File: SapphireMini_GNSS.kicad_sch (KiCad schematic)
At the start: 20 parts, among them J401 Conn_01x01_Male, U401 TPS22860DBVR, U402 SAM-M8Q-0-10

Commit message: Corrected to get clean review on schematic
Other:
- title: Sapphire Mini -> Sapphire Mini M2
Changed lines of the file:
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@@
   (paper "USLetter")
   (title_block
-    (title "Sapphire Mini")
+    (title "Sapphire Mini M2")
+    (date "2022-09-26")
+    (rev "1")
     (company "Southern Methodist Univ")
+    (comment 1 "Chris Hayward")
   )
   (junction (at 118.11 46.99) (diameter 0) (color 0 0 0 0)

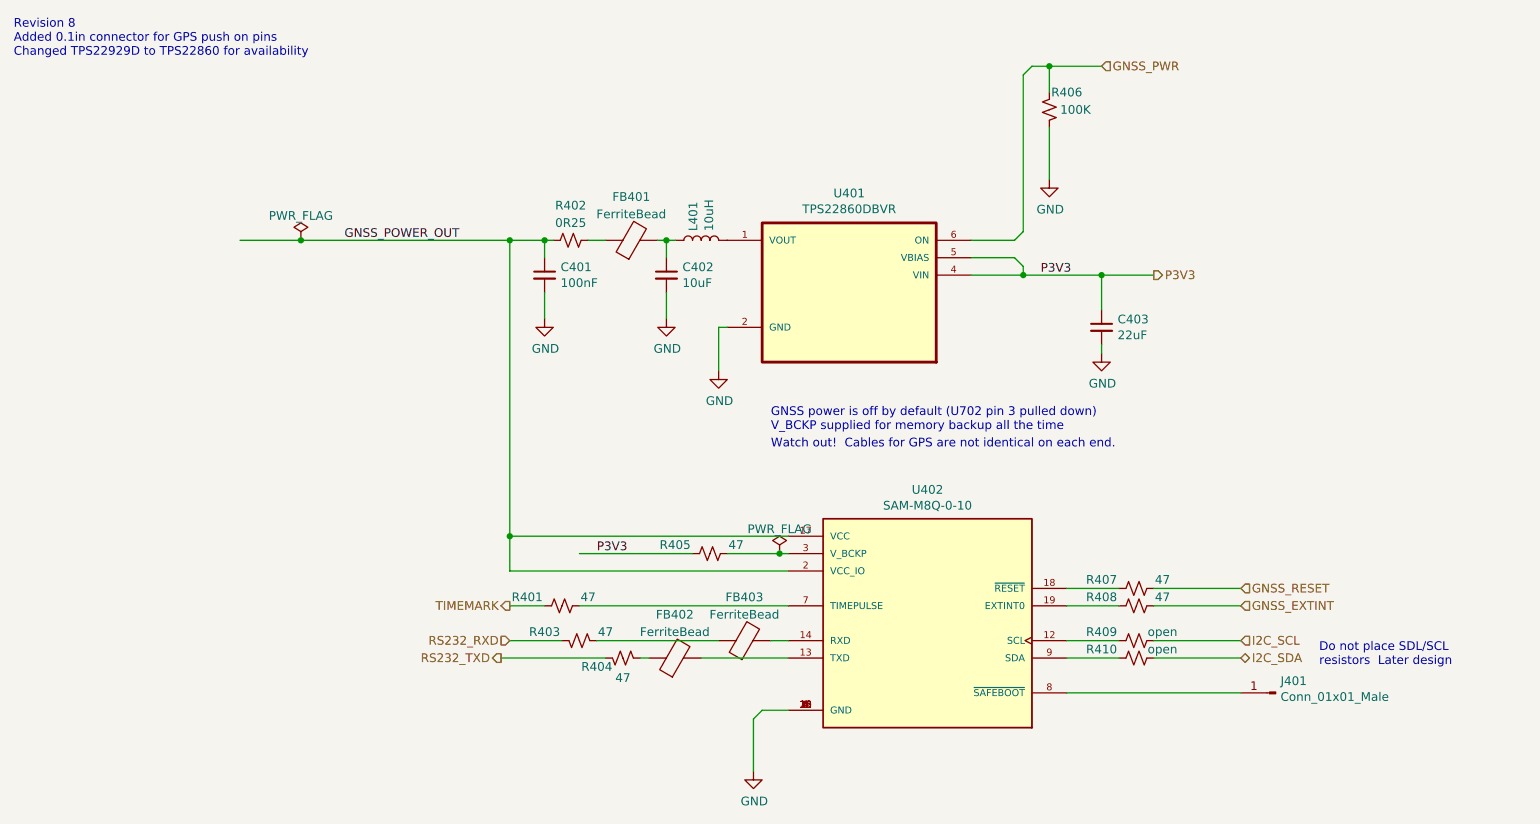
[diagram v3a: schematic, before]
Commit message: Footprints complete. Starting layout
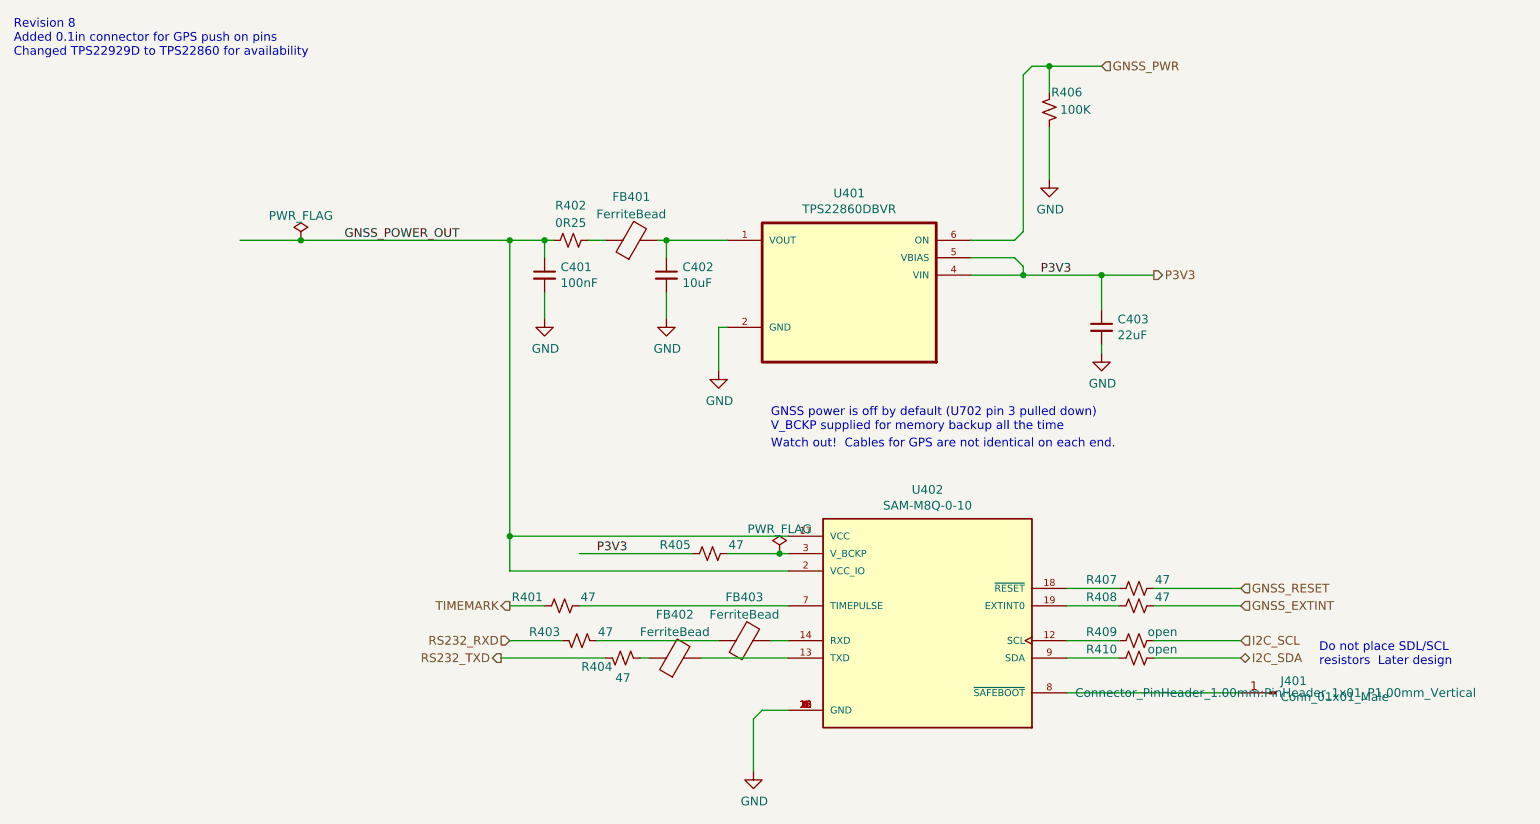
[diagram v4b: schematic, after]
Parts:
- removed L401: 10uH, symbol Device:L
- C401: MPN CL10B104KA8NNNC -> CL05A104KA5NNNC
- C402: MPN CL21B105KOFNNNG -> CL21A106KAYNNNE
- C403: MPN CGA5L1X5R1C226M160AC -> CL21A226MAYNNNE; Manufacturer TDK -> Samsung
- FB401, FB402, FB403: footprint (none) -> Inductor_SMD:L_0201_0603Metric; MPN (none) -> BLM18AG221SN1D
- J401: footprint (none) -> Connector_PinHeader_1.00mm:PinHeader_1x01_P1.00mm_Vertical; MPN (none) -> DNP
- U402: MPN (none) -> SAM-M8Q-0-10; Manufacturer (none) -> u-blox
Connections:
- net at C402.1, FB401.2: now also U401.1 (VOUT)
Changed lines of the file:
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@@
     (stroke (width 0) (type default) (color 0 0 0 0))
   )
-  (wire (pts (xy 118.11 46.99) (xy 119.38 46.99))
+  (wire (pts (xy 118.11 46.99) (xy 127 46.99))
     (stroke (width 0) (type default) (color 0 0 0 0))
   )
@@
       (effects (font (size 1.27 1.27)) hide)
     )
-    (property "MPN" "CL10B104KA8NNNC" (id 5) (at 100.33 52.07 0)
+    (property "MPN" "CL05A104KA5NNNC" (id 5) (at 100.33 52.07 0)
       (effects (font (size 1.27 1.27)) hide)
     )
@@
       (effects (font (size 1.27 1.27)) hide)
     )
-    (property "Description" "0.1 µF ±10% 25V Ceramic Capacitor X7R 0603 (1608 Metric)" (id 15) (at 100.33 52.07 0)
+    (property "Description" "0.1 µF ±10% 25V Ceramic Capacitor X5R 0402 (1005 Metric)" (id 15) (at 100.33 52.07 0)
       (effects (font (size 1.27 1.27)) hide)
     )
@@
       (effects (font (size 1.27 1.27)) hide)
     )
-    (property "MPN" "CGA5L1X5R1C226M160AC" (id 5) (at 181.61 59.69 0)
-      (effects (font (size 1.27 1.27)) hide)
-    )
-    (property "Manufacturer" "TDK" (id 6) (at 181.61 59.69 0)
+    (property "MPN" "CL21A226MAYNNNE" (id 5) (at 181.61 59.69 0)
+      (effects (font (size 1.27 1.27)) hide)
+    )
+    (property "Manufacturer" "Samsung" (id 6) (at 181.61 59.69 0)
       (effects (font (size 1.27 1.27)) hide)
     )
@@
       (effects (font (size 1.27 1.27)) hide)
     )
-    (property "Description" "22 µF ±20% 16V Ceramic Capacitor X5R 1206" (id 15) (at 181.61 59.69 0)
+    (property "Description" "22 µF ±20% 25V Ceramic Capacitor X5R 0805 (2012 Metric)" (id 15) (at 181.61 59.69 0)
       (effects (font (size 1.27 1.27)) hide)
     )
@@
       (effects (font (size 1.27 1.27)) hide)
     )
-    (property "MPN" "CL21B105KOFNNNG" (id 5) (at 118.11 52.07 0)
+    (property "MPN" "CL21A106KAYNNNE" (id 5) (at 118.11 52.07 0)
       (effects (font (size 1.27 1.27)) hide)
     )
@@
       (effects (font (size 1.27 1.27)) hide)
     )
-    (property "Description" "1 µF ±10% 16V Ceramic Capacitor X7R 0805 " (id 15) (at 118.11 52.07 0)
+    (property "Description" "10 µF ±10% 25V Ceramic Capacitor X5R 0805 (2012 Metric)" (id 15) (at 118.11 52.07 0)
       (effects (font (size 1.27 1.27)) hide)
     )
@@
     (property "MAXIMUM_PACKAGE_HEIGHT" "6.80mm" (id 7) (at 156.21 102.87 0)
       (effects (font (size 1.27 1.27)) (justify left bottom) hide)
+    )
+    (property "Description" "RF RX GALILEO 1.575GHZ/1.602GHZ" (id 8) (at 156.21 102.87 0)
+      (effects (font (size 1.27 1.27)) hide)
+    )
+    (property "MPN" "SAM-M8Q-0-10" (id 9) (at 156.21 102.87 0)
+      (effects (font (size 1.27 1.27)) hide)
+    )
+    (property "Manufacturer" "u-blox" (id 10) (at 156.21 102.87 0)
+      (effects (font (size 1.27 1.27)) hide)
     )
     (pin "1")
@@
       (effects (font (size 1.27 1.27)) (justify right))
     )
-    (property "Footprint" "" (id 2) (at 207.01 113.03 0)
-      (effects (font (size 1.27 1.27)) hide)
-    )
+    (property "Footprint" "Connector_PinHeader_1.00mm:PinHeader_1x01_P1.00mm_Vertical" (id 2) (at 207.01 113.03 0))
     (property "Datasheet" "~" (id 3) (at 207.01 113.03 0)
       (effects (font (size 1.27 1.27)) hide)
     )
-    (pin "1")
-  )
-  (symbol (lib_id "Device:L") (at 123.19 46.99 90) (unit 1)
-    (in_bom yes) (on_board yes)
-    (property "Reference" "L401" (id 0) (at 122.0216 45.6438 0)
-      (effects (font (size 1.27 1.27)) (justify left))
-    )
-    (property "Value" "10uH" (id 1) (at 124.333 45.6438 0)
-      (effects (font (size 1.27 1.27)) (justify left))
-    )
-    (property "Footprint" "" (id 2) (at 123.19 46.99 0)
-      (effects (font (size 1.27 1.27)) hide)
-    )
-    (property "Datasheet" "~" (id 3) (at 123.19 46.99 0)
-      (effects (font (size 1.27 1.27)) hide)
-    )
-    (pin "1")
-    (pin "2")
+    (property "Description" "PPS connector" (id 4) (at 207.01 113.03 0)
+      (effects (font (size 1.27 1.27)) hide)
+    )
+    (property "MPN" "DNP" (id 5) (at 207.01 113.03 0)
+      (effects (font (size 1.27 1.27)) hide)
+    )
+    (pin "1")
   )
   (symbol (lib_id "Device:R_Small_US") (at 104.14 46.99 90) (unit 1)
@@
     )
     (pin "1")
+  )
+  (symbol (lib_id "Device:FerriteBead") (at 129.54 105.41 90) (unit 1)
+    (in_bom yes) (on_board yes) (fields_autoplaced)
+    (property "Reference" "FB403" (id 0) (at 129.4892 99.0686 90))
+    (property "Value" "FerriteBead" (id 1) (at 129.4892 101.6055 90))
+    (property "Footprint" "Inductor_SMD:L_0201_0603Metric" (id 2) (at 129.54 107.188 90)
+      (effects (font (size 1.27 1.27)) hide)
+    )
+    (property "Datasheet" "~" (id 3) (at 129.54 105.41 0)
+      (effects (font (size 1.27 1.27)) hide)
+    )
+    (property "Description" "220 Ohms @ 100 MHz 1 Ferrite Bead 0603 (1608 Metric) 500mA 250mOhm" (id 4) (at 129.54 105.41 0)
+      (effects (font (size 1.27 1.27)) hide)
+    )
+    (property "MPN" "BLM18AG221SN1D" (id 5) (at 129.54 105.41 0)
+      (effects (font (size 1.27 1.27)) hide)
+    )
+    (pin "1")
+    (pin "2")
   )
   (symbol (lib_id "Device:FerriteBead") (at 113.03 46.99 90) (unit 1)
@@
     (property "Reference" "FB401" (id 0) (at 112.9792 40.6486 90))
     (property "Value" "FerriteBead" (id 1) (at 112.9792 43.1855 90))
-    (property "Footprint" "" (id 2) (at 113.03 48.768 90)
+    (property "Footprint" "Inductor_SMD:L_0201_0603Metric" (id 2) (at 113.03 48.768 90)
       (effects (font (size 1.27 1.27)) hide)
     )
@@
       (effects (font (size 1.27 1.27)) hide)
     )
-    (pin "1")
-    (pin "2")
-  )
-  (symbol (lib_id "Device:FerriteBead") (at 129.54 105.41 90) (unit 1)
-    (in_bom yes) (on_board yes) (fields_autoplaced)
-    (property "Reference" "FB403" (id 0) (at 129.4892 99.0686 90))
-    (property "Value" "FerriteBead" (id 1) (at 129.4892 101.6055 90))
-    (property "Footprint" "" (id 2) (at 129.54 107.188 90)
-      (effects (font (size 1.27 1.27)) hide)
-    )
-    (property "Datasheet" "~" (id 3) (at 129.54 105.41 0)
+    (property "Description" "220 Ohms @ 100 MHz 1 Ferrite Bead 0603 (1608 Metric) 500mA 250mOhm" (id 4) (at 113.03 46.99 0)
+      (effects (font (size 1.27 1.27)) hide)
+    )
+    (property "MPN" "BLM18AG221SN1D" (id 5) (at 113.03 46.99 0)
       (effects (font (size 1.27 1.27)) hide)
     )
@@
     (property "Reference" "FB402" (id 0) (at 119.3292 101.6086 90))
     (property "Value" "FerriteBead" (id 1) (at 119.3292 104.1455 90))
-    (property "Footprint" "" (id 2) (at 119.38 109.728 90)
+    (property "Footprint" "Inductor_SMD:L_0201_0603Metric" (id 2) (at 119.38 109.728 90)
       (effects (font (size 1.27 1.27)) hide)
     )
@@
       (effects (font (size 1.27 1.27)) hide)
     )
+    (property "Description" "220 Ohms @ 100 MHz 1 Ferrite Bead 0603 (1608 Metric) 500mA 250mOhm" (id 4) (at 119.38 107.95 0)
+      (effects (font (size 1.27 1.27)) hide)
+    )
+    (property "MPN" "BLM18AG221SN1D" (id 5) (at 119.38 107.95 0)
+      (effects (font (size 1.27 1.27)) hide)
+    )

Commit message: Working on update to power controllers
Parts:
- removed R401, R403, R404, R405, R407, R408: 47, Resistor_SMD:R_0603_1608Metric, symbol Device:R_Small_US
- removed R409, R410: open, Resistor_SMD:R_0603_1608Metric, symbol Device:R_Small_US
- added R401: EXB-2HV470JV, Sapphire:EXB-2HV470JV, symbol PanasonicRA:EXB-2HV470JV
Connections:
- net GNSS_EXTINT: now also R401.8
- net GNSS_RESET: now also R401.7
- net I2C_SCL: now also R401.4
- net I2C_SDA: now also R401.3
- net P3V3: now also R401.1
- net RS232_RXD: now also FB403.1
- net RS232_TXD: now also FB402.1
- net TIMEMARK: now also R401.2
- net TIMEPULSE: now reaches U402.7 (TIMEPULSE)
- net TIMEPULSE: now also R401.15
- net SAM_SCL: now reaches U402.12 (SCL)
- net SAM_SCL: now also R401.13
- net at FB402.2: now also R401.5; no longer U402.13 (TXD)
- net at FB403.2: now also R401.6; no longer U402.14 (RXD)
- net SAM_RESET: now reaches U402.18 (~{RESET})
- net SAM_RESET: now also R401.10
- net SAM_EXTINTO: now reaches U402.19 (EXTINT0)
- net SAM_EXTINTO: now also R401.9
- net V_BCKP: now reaches U402.3 (V_BCKP)
- net V_BCKP: now also R401.16
- net SAM_SDA: now reaches U402.9 (SDA)
- net SAM_SDA: now also R401.14
- new net SAM_RXD: R401.11, U402.14 (RXD)
- new net SAM_TXD: R401.12, U402.13 (TXD)
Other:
- moved on the sheet: FB402, FB403

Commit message: Checkpoint
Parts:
- removed C402: 10uF, Capacitor_SMD:C_0805_2012Metric, symbol Device:C_Small
- removed C403: 22uF, Capacitor_SMD:C_1206_3216Metric, symbol Device:C_Small
- removed FB401: FerriteBead, Inductor_SMD:L_0201_0603Metric, symbol Device:FerriteBead
- removed R402: 0R25, Resistor_SMD:R_0603_1608Metric, symbol Device:R_Small_US
- removed R406: 100K, Resistor_SMD:R_0603_1608Metric, symbol Device:R_Small_US
- removed U401: TPS22860DBVR, SOT95P280X145-6N, symbol sapphireMini:TPS22860DBVR
- U402: footprint MODULE_SAM-M8Q-0-10 -> SapphineMinimal:MODULE_SAM-M8Q-0-10
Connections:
- net GNSS_EXTINT: now also R401.7; no longer R401.8
- net GNSS_RESET: now also R401.8; no longer R401.7
- net I2C_SDA: now also R401.2; no longer R401.3
- net SAM_EXTINTO: now also R401.10; no longer R401.9
- net SAM_RESET: now also R401.9; no longer R401.10
- net SAM_SDA: now also R401.15; no longer R401.14
- net TIMEMARK: now also R401.3; no longer R401.2
- net TIMEPULSE: now also R401.14; no longer R401.15
- net GNSS_POWER_OUT renamed GNSS_OUTPUT_POWER
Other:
- note removed: "Watch out! Cables for GPS are not identical on each end."
- moved on the sheet: C401
